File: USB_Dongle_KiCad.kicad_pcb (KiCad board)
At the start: 6 copper layers, 72.4 x 29.2 mm, 52 parts, among them J1 USB_C_Receptacle_USB2.0, J2 Conn SWD 02x05, J3 DM3BT-DSF-PEJS, SW1 PCM12SMTR, SW2 KMR223G LFG, U1 AMS1117-3.3, U2 STULPI01A, U3 USBULC6-2M6, U4 ESDA14V2-2BF3, U5 STM32F730R8Tx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

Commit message: Updated: PCB design rules
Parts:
- moved C12 83.4 mm to (201.3, 89.1), turned to 180 degrees
- moved J2 83.1 mm to (210.3, 93.4), turned to -90 degrees
- moved C14 79.7 mm to (201.3, 84.6)
- moved C11 66.9 mm to (188.4, 75.1)
- moved C13 63.2 mm to (186.8, 73.4), turned to 180 degrees
- moved Y2 61.9 mm to (201.1, 86.9), turned to 90 degrees
- moved C26 54.0 mm to (183.3, 73.3), turned to -90 degrees
- moved SW2 47.6 mm to (179.5, 73.2), turned to 180 degrees
- moved R8 45.2 mm to (175.8, 73.2), turned to 90 degrees
- moved D2 23.4 mm to (176.5, 91.9)
- moved R5 23.4 mm to (179.6, 93.5)
- moved R6 23.4 mm to (179.6, 91.9)
- moved D1 23.4 mm to (176.5, 93.5)
- moved U1 3.22 mm to (168.2, 93.0)
- moved C3 3.22 mm to (162.7, 94.8)
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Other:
- board size 72.4 x 29.2 mm -> 63.6 x 27.1 mm

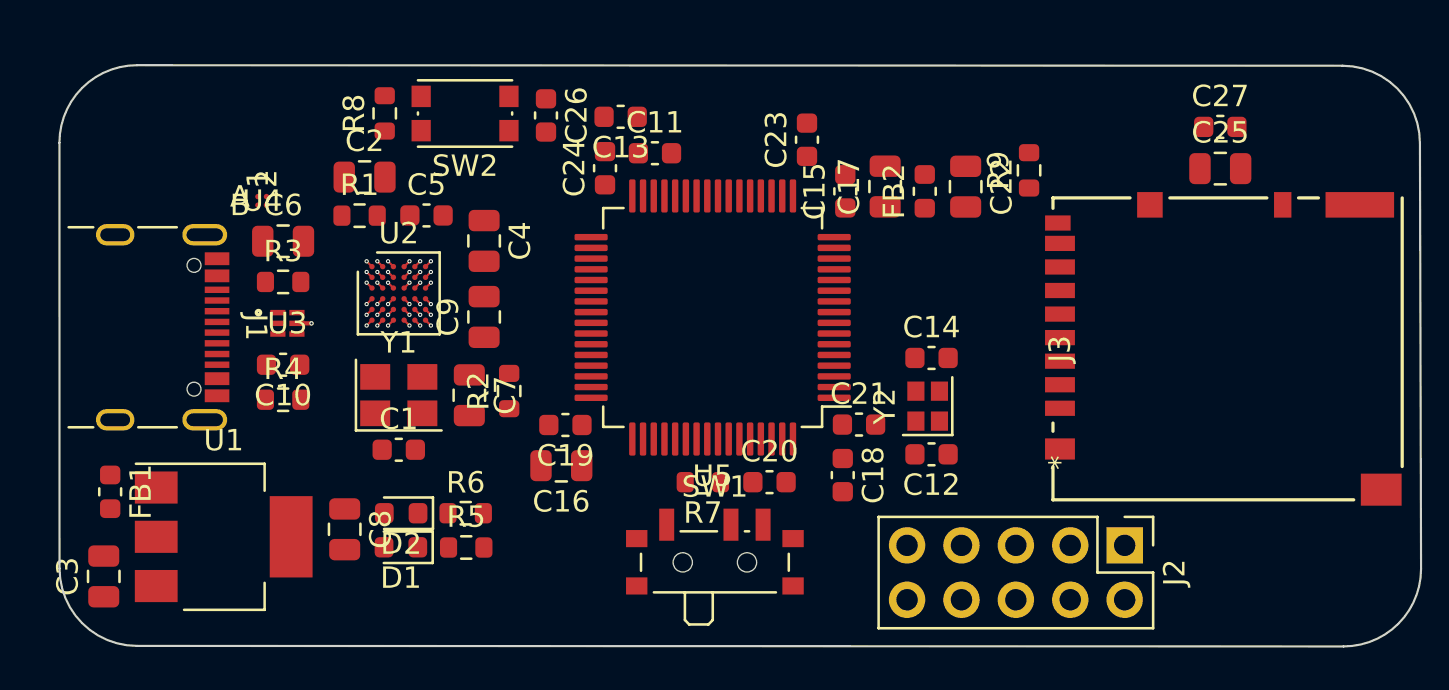
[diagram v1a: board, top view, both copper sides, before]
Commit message: Update: Routing of high speed tracks
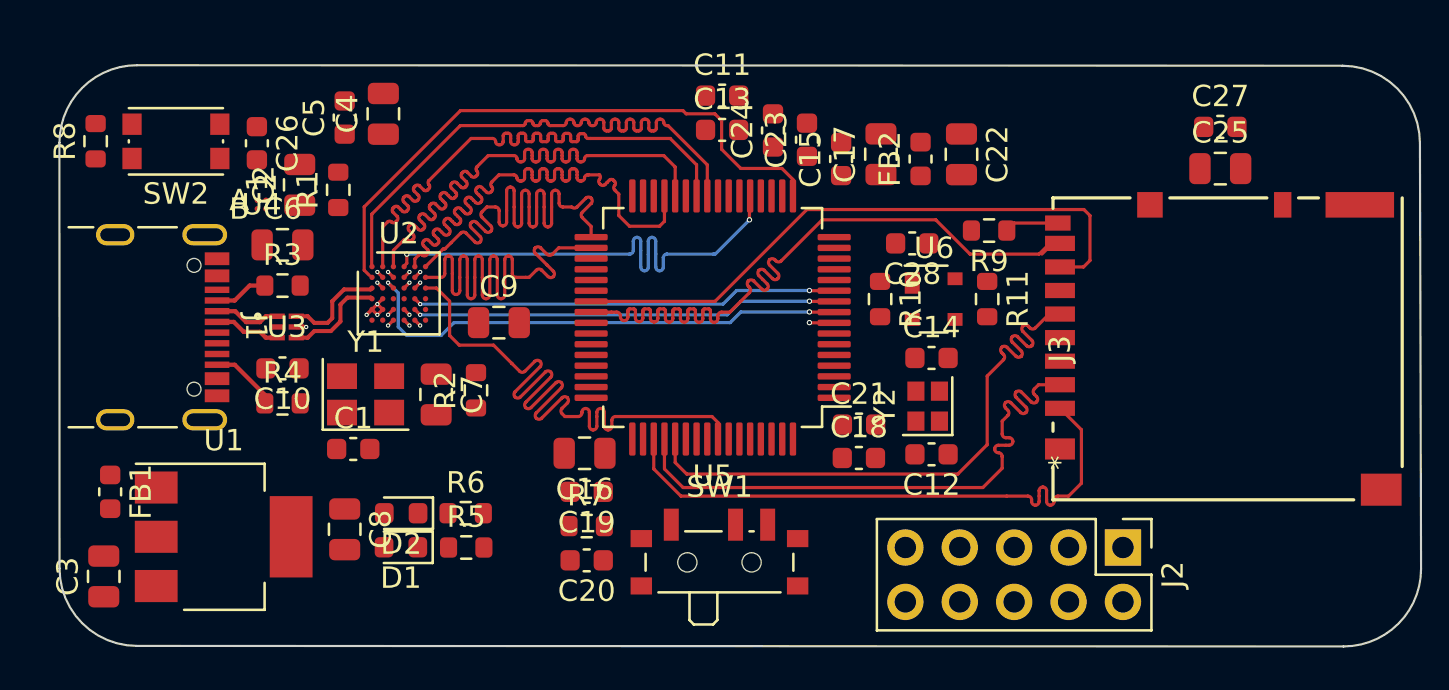
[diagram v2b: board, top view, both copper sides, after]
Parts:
- added C28: 100n, Capacitor_SMD:C_0603_1608Metric, F.Cu at (200.4, 79.3)
- added R10: 2.2k, Resistor_SMD:R_0603_1608Metric, F.Cu at (198.9, 81.9)
- added R11: 10k, Resistor_SMD:R_0603_1608Metric, F.Cu at (203.9, 81.9)
- added U6: CAT811TTBI-GT3, Package_TO_SOT_SMD:SOT-143, F.Cu at (201.4, 81.9)
- moved C26 13.6 mm to (169.8, 74.6)
- moved R8 13.6 mm to (162.3, 74.5)
- moved SW2 13.6 mm to (166.0, 74.5)
- moved C20 9.28 mm to (185.2, 94.1), turned to 180 degrees
- moved C24 8.04 mm to (193.9, 74.0)
- moved C4 7.57 mm to (175.7, 73.2), turned to 90 degrees
- moved C5 5.96 mm to (173.9, 73.4), turned to 90 degrees
- moved R7 5.80 mm to (185.2, 92.5), turned to 0 degrees
- moved C13 4.78 mm to (191.5, 74.0), turned to 0 degrees
- moved C11 4.13 mm to (191.5, 72.4)
- moved R9 3.37 mm to (204.0, 78.7), turned to 180 degrees
- moved C19 3.27 mm to (185.2, 90.9)
- moved C2 3.05 mm to (171.8, 76.6), turned to 90 degrees
- moved C1 2.13 mm to (174.3, 88.9)
- moved R1 1.56 mm to (173.6, 76.8), turned to 90 degrees
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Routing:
- net SDMMC_D1: track 0.00 -> 35.5 mm
- net ULPI_D7: track 0.35 -> 33.3 mm, vias 1 -> 0
- net SDMMC_D0: track 0.00 -> 28.8 mm
- net SDMMC_CLK: track 0.00 -> 28.0 mm
- net SDMMC_D2: track 0.00 -> 27.9 mm
- net SDMMC_D3: track 0.00 -> 27.9 mm
- net ULPI_D0: track 0.35 -> 28.1 mm, vias 1 -> 0
- net ULPI_D6: track 0.35 -> 26.8 mm, vias 1 -> 0
- net ULPI_D1: track 0.35 -> 26.8 mm, vias 1 -> 0
- net ULPI_D2: track 0.35 -> 26.8 mm, vias 1 -> 0
- net ULPI_D5: track 0.35 -> 26.8 mm, vias 1 -> 0
- net ULPI_D3: track 0.35 -> 26.7 mm, vias 1 -> 0
- net ULPI_D4: track 0.35 -> 26.7 mm, vias 1 -> 0
- net ULPI_CLK: track 0.35 -> 23.9 mm, vias 1 -> 2
- net ULPI_CS_PWR: track 0.35 -> 23.6 mm, vias 1 -> 2
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
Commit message: Update: near end of layout
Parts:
- moved R4 0.21 mm to (171.2, 86.8)
- turned C3 to -90 degrees
- turned Y2 to 0 degrees
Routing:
- net VBUS: track 0.00 -> 76.5 mm, vias 0 -> 2
- net NRST: track 0.00 -> 60.1 mm, vias 0 -> 2
- net +3.3V: track 1.41 -> 53.3 mm, vias 4 -> 27
- net GND: track 3.51 -> 52.5 mm, vias 6 -> 45
- net SWCLK: track 0.00 -> 30.2 mm, vias 0 -> 1
- net SWDIO: track 0.00 -> 29.1 mm, vias 0 -> 1
- net ULPI_STP: track 1.16 -> 23.4 mm, vias 1 -> 2
- net SDMMC_CMD: track 0.00 -> 20.9 mm, vias 0 -> 2
- net ULPI_RESET: track 0.35 -> 21.1 mm, vias 1 -> 2
- net SWO: track 0.00 -> 19.9 mm, vias 0 -> 1
- net Net-(SW1-B): track 0.00 -> 17.5 mm
- net Net-(U2-RREF): track 0.35 -> 13.9 mm, vias 1 -> 2
- net BOOT0: track 0.00 -> 11.5 mm, vias 0 -> 2
- net SDMMC_CDS: track 2.53 -> 13.9 mm, vias 0 -> 2
- net Net-(U2-VBUS): track 0.35 -> 10.6 mm, vias 1 -> 2
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- added copper zone on In3.Cu, net +3.3V
- added copper zone on B.Cu, net GND
- added copper zone on F.Cu, net GND
- added copper zone on In1.Cu, net GND
- added copper zone on In4.Cu, net GND

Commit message: Various fixes and other 3D models added
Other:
- board text added: "3.3V"
- board text added: "5V"
- board text added: "Boot SW"
- board text added: "GND"
- board text added: "LEDs"
- board text added: "Regulator"
- board text added: "Reset SW"
- board text added: "STM32"
- board text added: "SWD"
- board text added: "ULPI"
- board text added: "USB-C"
- board text added: "microSD"

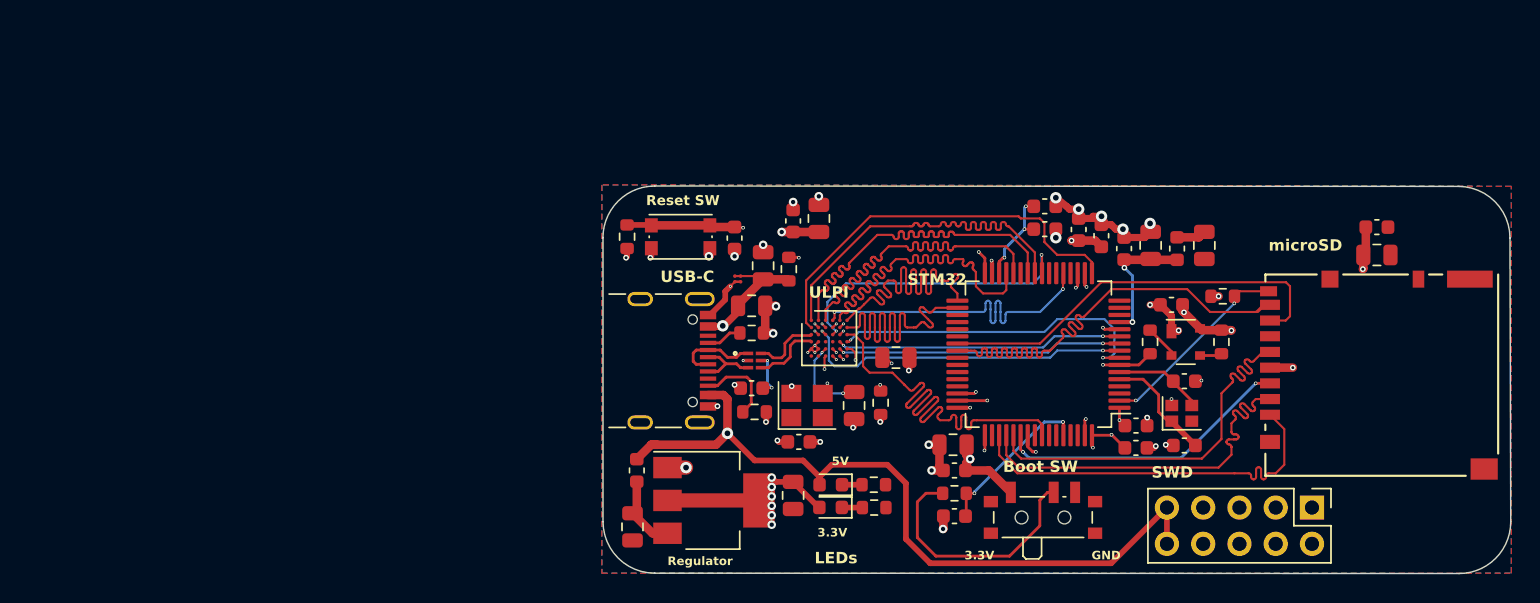
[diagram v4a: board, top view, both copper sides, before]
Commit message: Update: New routing after ULPI component change
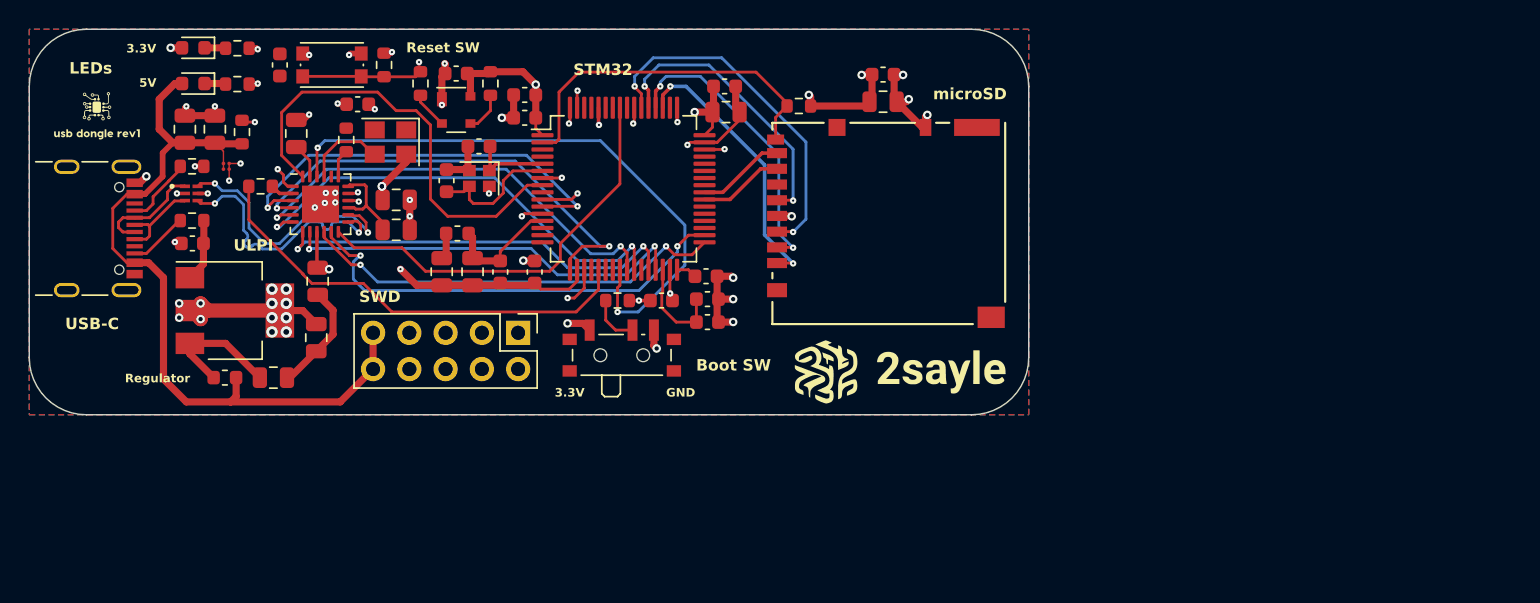
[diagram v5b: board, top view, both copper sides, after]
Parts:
- added G***: LOGO, LOGO, F.Cu at (181.4, 84.0)
- added G***: LOGO, LOGO, F.Cu at (125.2, 66.0)
- added R12: 2.2k, Resistor_SMD:R_0603_1608Metric, F.Cu at (147.8, 63.8)
- C25: value 10u -> 100n; footprint Capacitor_SMD:C_0805_2012Metric -> Capacitor_SMD:C_0603_1608Metric
- C26: value 47n -> 10u; footprint Capacitor_SMD:C_0603_1608Metric -> Capacitor_SMD:C_0805_2012Metric
- C27: value 100n -> 47n
- C5: value 100n -> 1u; footprint Capacitor_SMD:C_0603_1608Metric -> Capacitor_SMD:C_0805_2012Metric
- C6: value 1u -> 22u
- C7: value 1.5u -> 1u
- C8: value 22u -> 1u
- C9: value 1.5u -> 100n
- R1: value 2.2k -> 20k
- R10: value 2.2k -> 10k
- R2: value 12k -> 8.06k
- R6: value 1k -> 22R
- R7: value 10k -> 1k
- R8: value 4.7k -> 10k
- R9: value 10k -> 4.7k
- U2: value STULPI01A -> USB3343; footprint Package_BGA:ST_uTFBGA-36_3.6x3.6mm_Layout6x6_P0.5mm -> Package_DFN_QFN:QFN-24-1EP_4x4mm_P0.5mm_EP2.6x2.6mm
- Y1: value 3225 SMD Oscillator -> 26 MHz
- moved C27 77.7 mm to (137.9, 62.5), turned to 90 degrees
- moved C25 65.7 mm to (150.3, 63.1), turned to 180 degrees
- moved R9 60.9 mm to (145.2, 62.5), turned to -90 degrees
- moved R7 57.8 mm to (135.0, 63.8)
- moved J2 56.9 mm to (154.6, 81.3)
- moved D1 55.0 mm to (131.9, 61.3)
- moved R5 55.0 mm to (135.0, 61.3)
- moved C12 53.7 mm to (151.9, 68.2)
- moved U6 53.6 mm to (150.3, 65.7)
- moved C14 53.6 mm to (149.6, 70.6), turned to 90 degrees
- moved C22 53.4 mm to (149.3, 77.0)
- moved D2 52.8 mm to (131.9, 63.8)
- moved Y2 51.9 mm to (151.9, 70.5), turned to 180 degrees
- moved FB2 50.4 mm to (150.4, 74.3), turned to 180 degrees
- moved R10 49.6 mm to (152.7, 63.8)
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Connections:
- C26 pad 1: NRST -> +3.3V
- C27 pad 1: +3.3V -> NRST
- C4 pad 1: +3.3V -> GND
- C4 pad 2: GND -> +3.3V
- C5 pad 1: +3.3V -> VBUS
- C6 pad 1: VBUS -> +3.3V
- C7 pad 1: Net-(U2-3V3V) -> Net-(U2-ID)
- C8 pad 1: +3.3V -> Net-(U2-VDD18)
- C9 pad 1: Net-(U2-1V2V) -> +3.3V
- R10 pad 1: Net-(U6-~{RESET}) -> +3.3V
- R10 pad 2: NRST -> Net-(U6-~{MR})
- R11 pad 1: +3.3V -> SDMMC_CDS
- R11 pad 2: Net-(U6-~{MR}) -> +3.3V
- R2 pad 2: Net-(U2-RREF) -> Net-(U2-RBIAS)
- R6 pad 1: Net-(D2-K) -> Net-(U2-CLKOUT)
- R6 pad 2: GND -> ULPI_CLK
- R7 pad 1: Net-(SW1-B) -> Net-(D2-K)
- R7 pad 2: BOOT0 -> GND
- R8 pad 1: +3.3V -> Net-(SW1-B)
- R8 pad 2: NRST -> BOOT0
- R9 pad 1: SDMMC_CDS -> +3.3V
- R9 pad 2: +3.3V -> NRST
- Y1 pad 3: Net-(U2-XI) -> Net-(U2-REFCLK/XI)
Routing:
- net SDMMC_D1: track 35.5 -> 6.22 mm
- net GND: track 52.5 -> 77.0 mm, vias 45 -> 36
- net ULPI_CS_PWR: track 23.6 -> 0.00 mm, vias 2 -> 0
- net SDMMC_D0: track 28.8 -> 5.97 mm
- net NRST: track 60.1 -> 38.1 mm
- net VBUS: track 76.5 -> 54.6 mm, vias 2 -> 0
- net ULPI_RESET: track 21.1 -> 42.3 mm
- net Net-(SW1-B): track 17.5 -> 3.54 mm
- net Net-(U2-RREF): track 13.9 -> 0.00 mm, vias 2 -> 0
- net USB_D-: track 4.76 -> 18.4 mm, vias 0 -> 2
- net USB_D+: track 4.76 -> 18.3 mm, vias 0 -> 2
- net SWO: track 19.9 -> 32.4 mm
- net SDMMC_CDS: track 13.9 -> 24.9 mm, vias 2 -> 0
- net ULPI_DIR: track 20.0 -> 30.6 mm
- net ULPI_NXT: track 20.1 -> 29.6 mm
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- added copper zone on In2.Cu, net GND
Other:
- board size 63.6 x 27.1 mm -> 70 x 27 mm

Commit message: Improved layout
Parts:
- moved G*** 0.58 mm to (124.7, 66.3)
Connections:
- J1 pad S1: unconnected-(J1-SHIELD-PadS1) -> (no net)
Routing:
- net SDMMC_D0: track 5.97 -> 30.5 mm
- net SDMMC_D1: track 6.22 -> 28.9 mm, vias 0 -> 2
- net SDMMC_D2: track 19.5 -> 28.7 mm
- net SDMMC_CLK: track 20.1 -> 28.7 mm
- net SDMMC_D3: track 20.7 -> 28.7 mm
- net ULPI_D3: track 29.0 -> 35.6 mm
- net ULPI_D7: track 29.4 -> 35.8 mm
- net ULPI_CLK: track 31.6 -> 35.9 mm
- net GND: track 77.0 -> 81.2 mm, vias 36 -> 45
- net ULPI_D4: track 28.7 -> 32.7 mm
- net SDMMC_CMD: track 25.2 -> 28.7 mm
- net ULPI_D5: track 30.0 -> 33.2 mm
- net ULPI_RESET: track 42.3 -> 44.7 mm
- net ULPI_D1: track 31.2 -> 32.9 mm
- net NRST: track 38.1 -> 39.7 mm
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
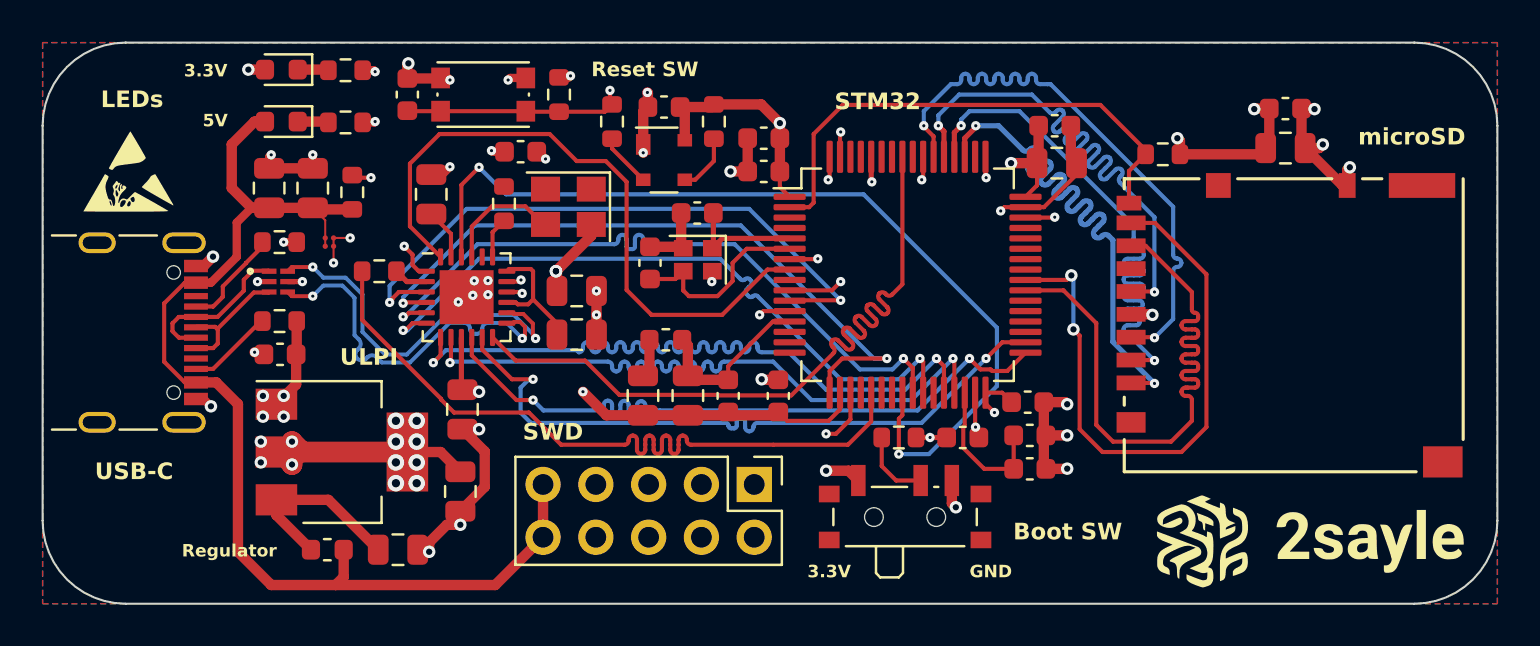
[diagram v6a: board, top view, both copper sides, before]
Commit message: Added: 3D screenshot
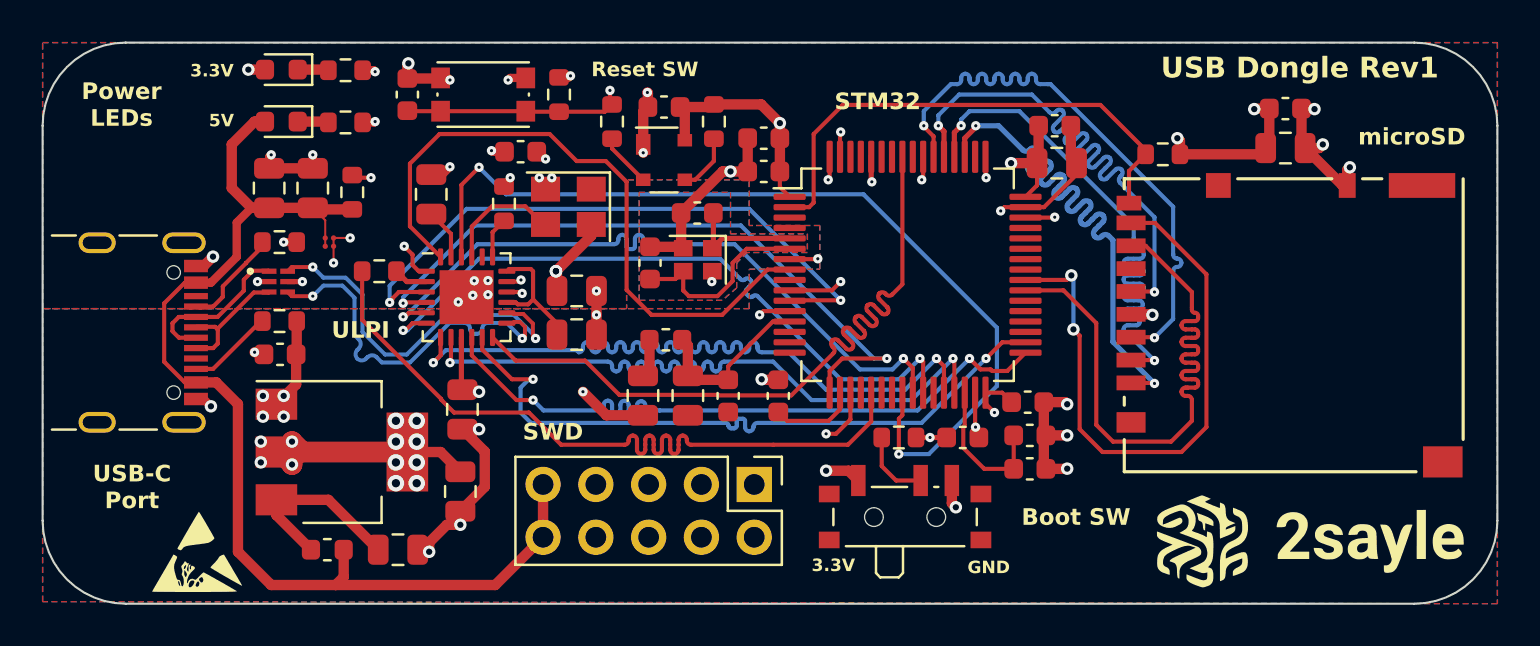
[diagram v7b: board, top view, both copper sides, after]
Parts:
- moved G*** 18.6 mm to (128.0, 84.6)
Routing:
- net GND: track 81.2 -> 83.7 mm, vias 45 -> 48
- net NRST: track 39.7 -> 41.9 mm
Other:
- board text added: "Power LEDs"
- board text added: "USB Dongle Rev1"
- board text added: "USB-C Port"
- board text removed: "LEDs"
- board text removed: "Regulator"
- board text removed: "USB-C"

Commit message: Small changes
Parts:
- moved C11 52.1 mm to (117.1, 67.3)
- moved C13 52.1 mm to (117.1, 68.9)
- moved R4 52.1 mm to (81.0, 61.8)
- moved U1 52.1 mm to (84.0, 68.1)
- moved U6 52.1 mm to (99.5, 54.0)
- moved C1 52.1 mm to (92.6, 53.6)
- moved C12 52.1 mm to (101.1, 56.6)
- moved C18 52.1 mm to (117.0, 65.7)
- moved C19 52.1 mm to (105.0, 65.4)
- moved C2 52.1 mm to (82.6, 55.4)
- moved C20 52.1 mm to (113.9, 67.4)
- moved C25 52.1 mm to (99.5, 51.5)
- moved C26 52.1 mm to (129.4, 53.5)
- moved C28 52.1 mm to (129.4, 51.6)
- moved C5 52.1 mm to (80.5, 55.4)
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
